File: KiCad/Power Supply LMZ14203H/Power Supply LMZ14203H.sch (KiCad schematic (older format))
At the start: 38 parts, among them J1 Power IN, J2 Conn_02x03_Odd_Even, J3 Power OUT, U1 INA169, U3 MCP3428, U4 INA169

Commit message: CPU added
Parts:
- removed C5: 10u, Capacitors_THT:CP_Radial_D6.3mm_P2.50mm, symbol CP
- removed C6: 100n, Capacitors_SMD:C_0805, symbol C
- removed C?: 47u/1-45mESR, Capacitors_THT:CP_Radial_D8.0mm_P2.50mm, symbol CP
- removed R10, R11, R8, R9: 0, Resistors_SMD:R_0805, symbol R
- removed U3: MCP3428, Housings_SOIC:SOIC-14_3.9x8.7mm_Pitch1.27mm, symbol MCP3428
- added C10, C11, C9: 47u/1-45mESR, Capacitors_SMD:C_1206, symbol C
- added C? (x2): 100nC, symbol C
- added C? (x2): 10u, symbol CP
- added J?: PDI, symbol Conn_02x03_Odd_Even
- added J?: OLED I2C, symbol Conn_01x04
- added L?: 10u, symbol L
- added R?: 10k, Resistors_SMD:R_0805, symbol R
- added R? (x2): 2k2, Resistors_SMD:R_0805, symbol R
- added U?: ATXMEGA32E5-AU, TQFP32, symbol ATXMEGA32E5-AU
- C1: footprint Capacitors_THT:CP_Radial_D8.0mm_P2.50mm -> Capacitors_SMD:CP_Elec_6.3x7.7
- C2: renamed from C?; footprint Capacitors_SMD:C_0805 -> Capacitors_SMD:C_1206
- U2: renamed from U?; footprint (none) -> TO_SOT_Packages_SMD:TO-263-7_TabPin4
- gave numbers to parts that had none: 7
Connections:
- net labels added: +3.3V, GND, PDI_CLK, PDI_DATA, SCK
- wire segments 79 -> 98
- no-connect marks 0 -> 2
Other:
- note removed: "Uref=2024mV"
- moved on the sheet: C1, C2, C3, C4, C7, C8, J1, J2, J3, R1, R12, R13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

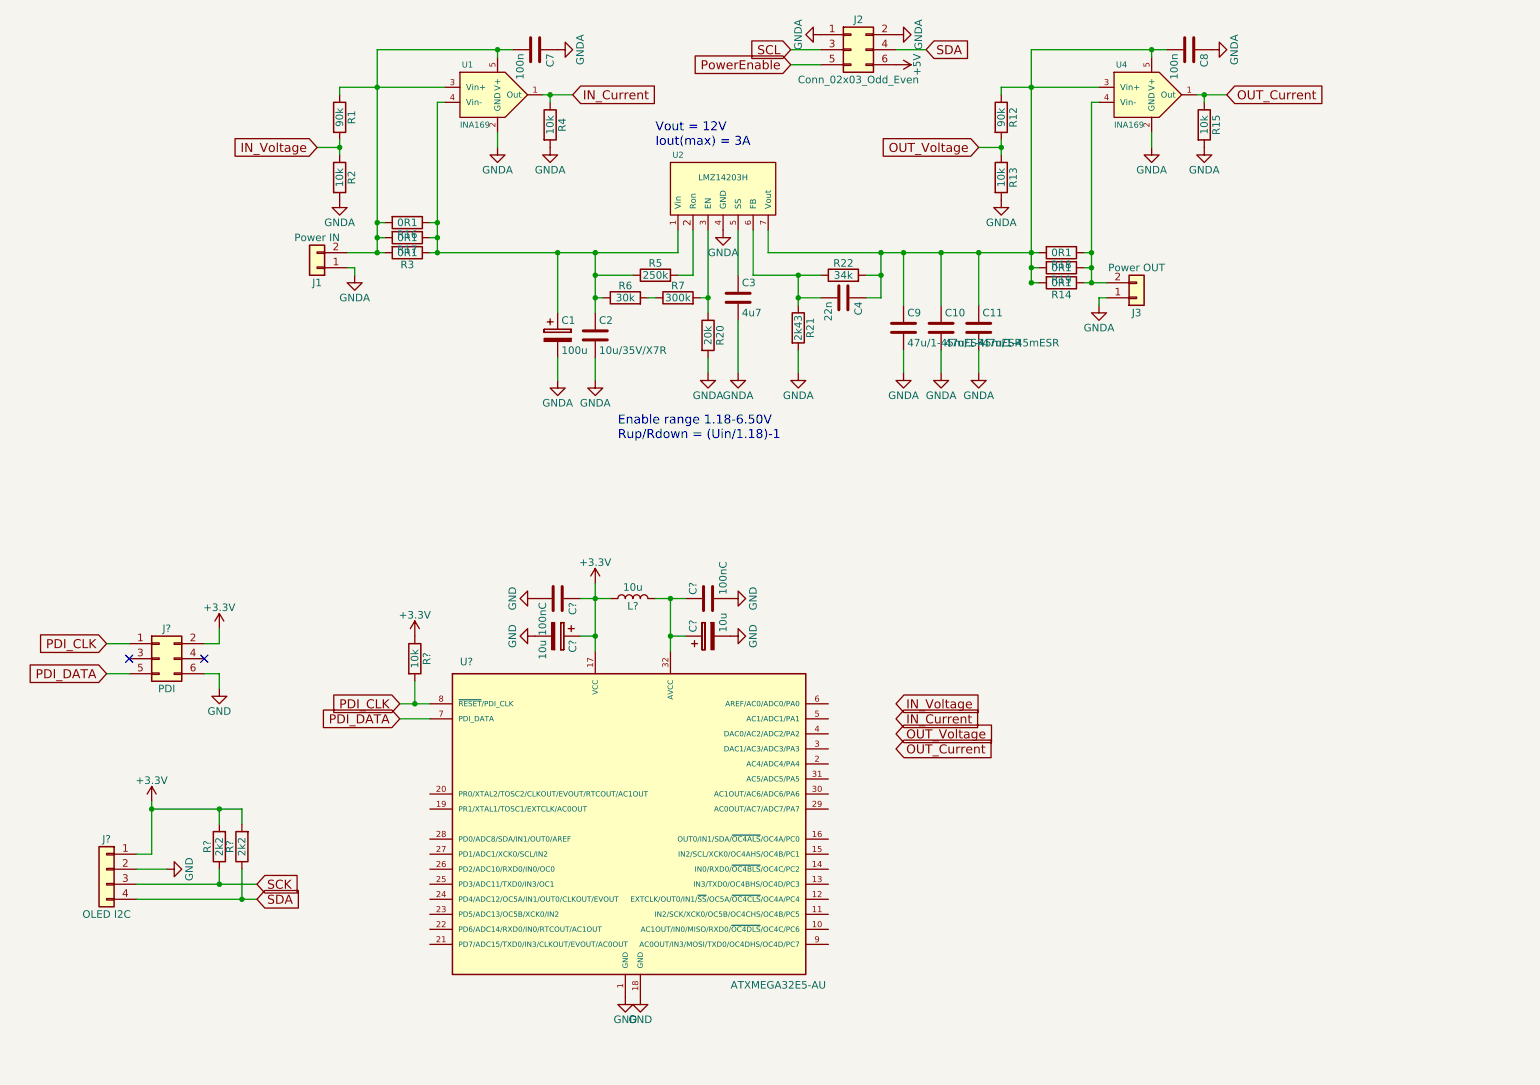
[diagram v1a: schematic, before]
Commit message: CPU added
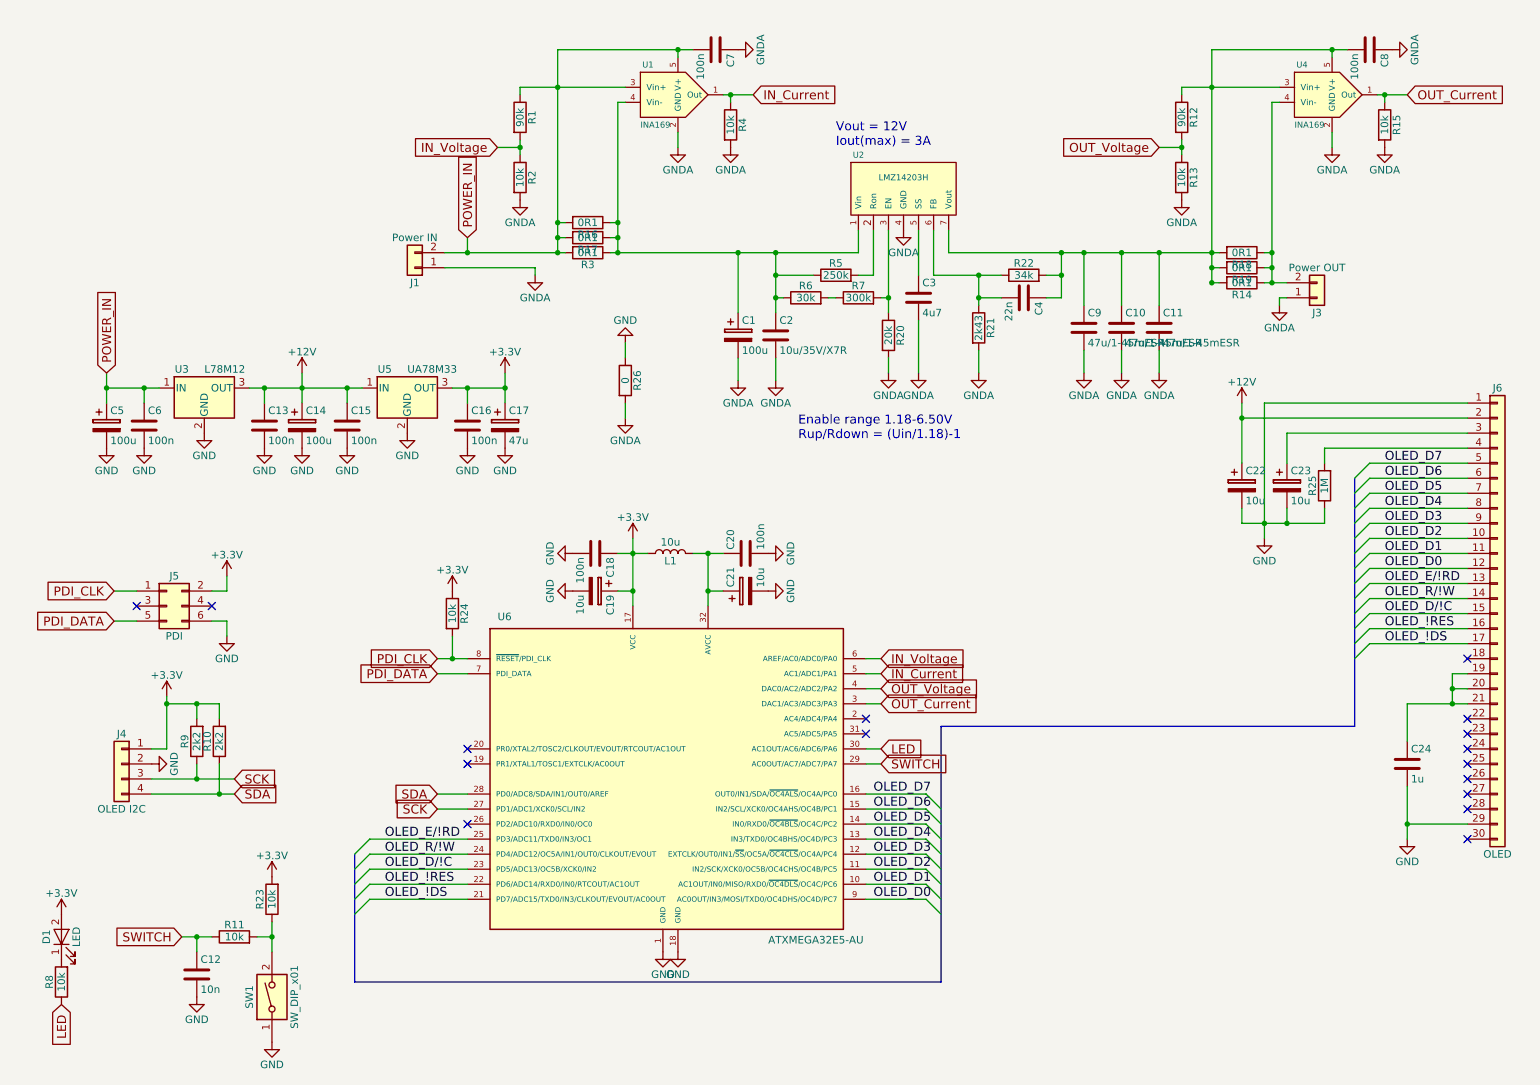
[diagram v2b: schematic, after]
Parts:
- removed J2: Conn_02x03_Odd_Even, Pin_Headers:Pin_Header_Straight_2x03_Pitch2.54mm, symbol Conn_02x03_Odd_Even
- added C12: 10n, Capacitors_SMD:C_0805, symbol C
- added C13, C15, C16, C6: 100n, Capacitors_SMD:C_0805, symbol C
- added C14: 100u, Capacitors_SMD:CP_Elec_6.3x7.7, symbol CP
- added C17: 47u, Capacitors_SMD:CP_Elec_6.3x5.8, symbol CP
- added C22, C23: 10u, Capacitors_SMD:CP_Elec_4x5.8, symbol CP
- added C24: 1u, Capacitors_SMD:C_0805, symbol C
- added C5: 100u, Capacitors_SMD:C_0805, symbol CP
- added D1: LED, Diodes_SMD:D_0805, symbol LED
- added J6: OLED, symbol Conn_01x30
- added R11, R23, R8: 10k, Resistors_SMD:R_0805, symbol R
- added R25: 1M, Resistors_SMD:R_0805, symbol R
- added R26: 0, Resistors_SMD:R_0805, symbol R
- added SW1: SW_DIP_x01, symbol SW_DIP_x01
- added U3: L78M12, symbol L7805
- added U5: UA78M33, symbol L7805
- C18, C20: renamed from C?; value 100nC -> 100n; footprint (none) -> Capacitors_SMD:C_0805
- C19, C21: renamed from C?; footprint (none) -> Capacitors_SMD:CP_Elec_4x5.8
- J4: renamed from J?; footprint (none) -> Pin_Headers:Pin_Header_Straight_1x04_Pitch2.54mm
- J5: renamed from J?; footprint (none) -> Pin_Headers:Pin_Header_Straight_2x03_Pitch2.54mm
- gave numbers to parts that had none: 5
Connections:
- net +3V3: now also C16.1, C17.1, D1.2 (A), R23.2, U5.3 (OUT)
- net GND: now also C12.2, C13.2, C14.2, C15.2, C16.2, C17.2, C22.2, C23.2, C24.2, C5.2, C6.2, J6.1 (Pin_1), J6.29 (Pin_29), R25.1, R26.1, SW1.1, U3.2 (GND), U5.2 (GND)
- net GNDA: now also R26.2
- net IN_Current: now also U6.5 (AC1/ADC1/PA1)
- net IN_Voltage: now also U6.6 (AREF/AC0/ADC0/PA0)
- net OUT_Current: now also U6.3 (DAC1/AC3/ADC3/PA3)
- net OUT_Voltage: now also U6.4 (DAC0/AC2/ADC2/PA2)
- net SCK: now also U6.27 (PD1/ADC1/XCK0/SCL/IN2)
- net SDA: now also U6.28 (PD0/ADC8/SDA/IN1/OUT0/AREF)
- net POWER_IN: now reaches C7.2, J1.2 (Pin_2), R1.1, R16.2, R17.2, R3.2, U1.3 (Vin+), U1.5 (V+)
- net POWER_IN: now also C5.1, C6.1, U3.1 (IN)
- net OLED_D1: now reaches U6.10 (AC1OUT/IN0/MISO/RXD0/~OC4DLS~/OC4C/PC6)
- net OLED_D1: now also J6.11 (Pin_11)
- net OLED_D2: now reaches U6.11 (IN2/SCK/XCK0/OC5B/OC4CHS/OC4B/PC5)
- net OLED_D2: now also J6.10 (Pin_10)
- net OLED_D3: now reaches U6.12 (EXTCLK/OUT0/IN1/~SS~/OC5A/~OC4CLS~/OC4A/PC4)
- net OLED_D3: now also J6.9 (Pin_9)
- net OLED_D4: now reaches U6.13 (IN3/TXD0/OC4BHS/OC4D/PC3)
- net OLED_D4: now also J6.8 (Pin_8)
- net OLED_D5: now reaches U6.14 (IN0/RXD0/~OC4BLS~/OC4C/PC2)
- net OLED_D5: now also J6.7 (Pin_7)
- net OLED_D6: now reaches U6.15 (IN2/SCL/XCK0/OC4AHS/OC4B/PC1)
- net OLED_D6: now also J6.6 (Pin_6)
- net OLED_D7: now reaches U6.16 (OUT0/IN1/SDA/~OC4ALS~/OC4A/PC0)
- net OLED_D7: now also J6.5 (Pin_5)
- net OLED_!DS: now reaches U6.21 (PD7/ADC15/TXD0/IN3/CLKOUT/EVOUT/AC0OUT)
- net OLED_!DS: now also J6.17 (Pin_17)
- net OLED_!RES: now reaches U6.22 (PD6/ADC14/RXD0/IN0/RTCOUT/AC1OUT)
- net OLED_!RES: now also J6.16 (Pin_16)
- net OLED_D/!C: now reaches U6.23 (PD5/ADC13/OC5B/XCK0/IN2)
- net OLED_D/!C: now also J6.15 (Pin_15)
- net OLED_R/!W: now reaches U6.24 (PD4/ADC12/OC5A/IN1/OUT0/CLKOUT/EVOUT)
- net OLED_R/!W: now also J6.14 (Pin_14)
- net OLED_E/!RD: now reaches U6.25 (PD3/ADC11/TXD0/IN3/OC1)
- net OLED_E/!RD: now also J6.13 (Pin_13)
- net SWITCH: now reaches U6.29 (AC0OUT/AC7/ADC7/PA7)
- net SWITCH: now also C12.1, R11.1
- net LED: now reaches U6.30 (AC1OUT/AC6/ADC6/PA6)
- net LED: now also R8.1
- net OLED_D0: now reaches U6.9 (AC0OUT/IN3/MOSI/TXD0/OC4DHS/OC4D/PC7)
- net OLED_D0: now also J6.12 (Pin_12)
- new net: D1.1 (K), R8.2
- new net: R11.2, R23.1, SW1.2
- new net: C24.1, J6.19 (Pin_19), J6.20 (Pin_20), J6.21 (Pin_21)
- new net: C23.1, J6.3 (Pin_3)
- new net: J6.4 (Pin_4), R25.2
- new net +12V: C13.1, C14.1, C15.1, C22.1, J6.2 (Pin_2), U3.3 (OUT), U5.1 (IN)
- no-connect marks 2 -> 16
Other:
- moved on the sheet: C1, C10, C11, C18, C19, C2, C20, C21, C3, C4, C7, C8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
